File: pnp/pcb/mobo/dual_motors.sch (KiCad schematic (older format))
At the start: 9 parts, among them M5 MOTOR1, M6 MOTOR2

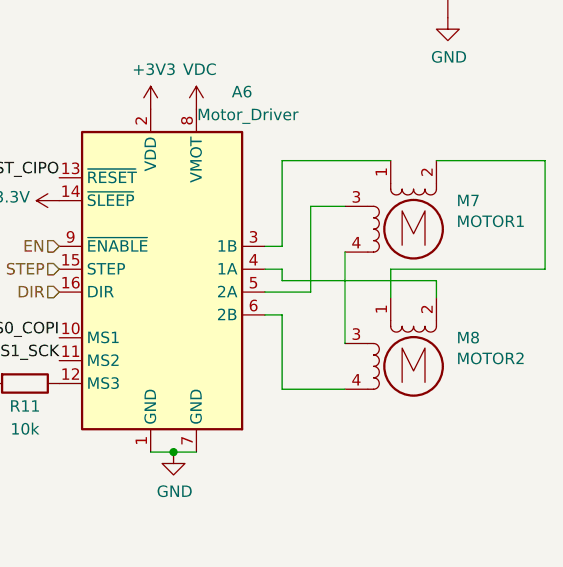
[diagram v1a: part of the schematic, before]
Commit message: Reversed Y and A stepper motor connector
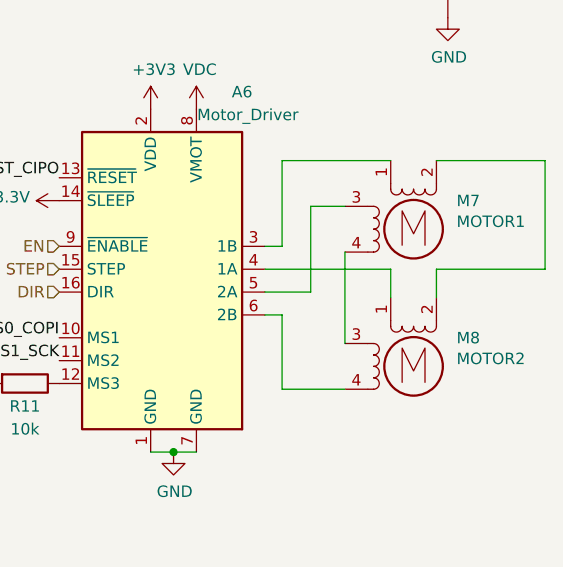
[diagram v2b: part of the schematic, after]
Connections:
- net at M6.1: now also A5.4 (1A); no longer M5.2 (-)
- net at M6.2 (-): now also M5.2 (-); no longer A5.4 (1A)
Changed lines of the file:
@@
 	5725 3250 5925 3250
-Wire Wire Line
-	5800 3150 5725 3150
-Wire Wire Line
-	5800 3200 5800 3150
-Wire Wire Line
-	6475 3200 5800 3200
-Wire Wire Line
-	6475 3275 6475 3200
-Wire Wire Line
-	6275 3150 6275 3275
-Wire Wire Line
-	6950 3150 6275 3150
 Wire Wire Line
 	6950 2675 6950 3150
@@
 	0    1    1    0
 $EndComp
+Wire Wire Line
+	6950 3150 6475 3150
+Wire Wire Line
+	6475 3150 6475 3275
+Wire Wire Line
+	6275 3275 6275 3150
+Wire Wire Line
+	5725 3150 6275 3150
 $EndSCHEMATC

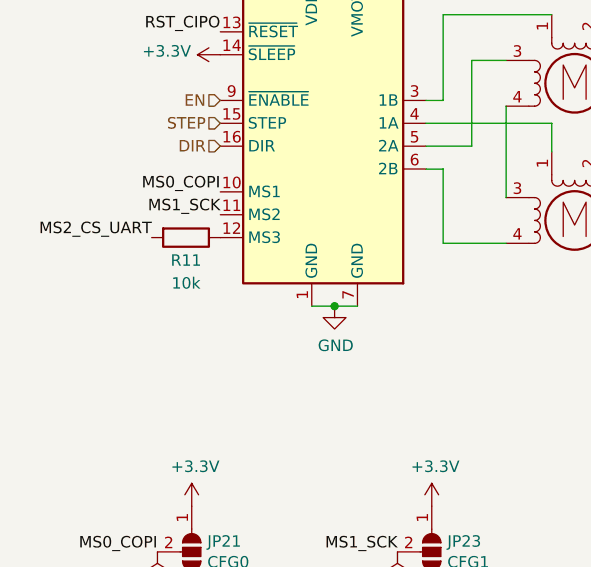
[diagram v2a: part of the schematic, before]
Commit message: Change TMC resistors to 1K
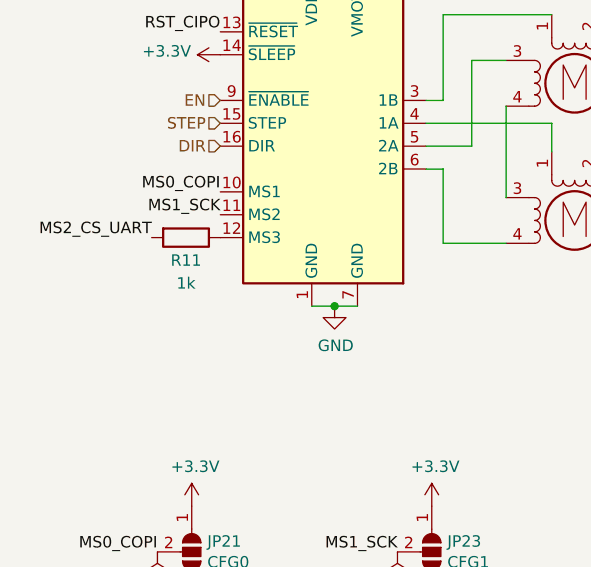
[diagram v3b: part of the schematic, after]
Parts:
- R10: value 10k -> 1k; Digikey RMCF0805FT10K0CT-ND -> (none); JLCPCB C17414 -> C17855; LCSC C115295 -> C322766; Mouser 71-CRCW080510K0FKEAC -> (none)
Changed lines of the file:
@@
 $EndDescr
-$Comp
-L Device:R R?
-U 1 1 6057EB7D
-P 4675 3650
-AR Path="/5EB0C248/6057EB7D" Ref="R?"  Part="1"
-AR Path="/5EB0C248/6057B851/6057EB7D" Ref="R10"  Part="1"
-AR Path="/5EB0C248/60582104/6057EB7D" Ref="R11"  Part="1"
-F 0 "R11" V 4775 3650 50  0000 C CNN
-F 1 "10k" V 4875 3650 50  0000 C CNN
-F 2 "Resistor_SMD:R_0805_2012Metric" V 4605 3650 50  0001 C CNN
-F 3 "" H 4675 3650 50  0001 C CNN
-F 4 "RMCF0805FT10K0CT-ND" H 4675 3650 50  0001 C CNN "Digikey"
-F 5 "C17414" H 4675 3650 50  0001 C CNN "JLCPCB"
-F 6 "C115295" H 4675 3650 50  0001 C CNN "LCSC"
-F 7 "71-CRCW080510K0FKEAC" H 4675 3650 50  0001 C CNN "Mouser"
-	1    4675 3650
-	0    1    1    0
-$EndComp
 $Comp
 L power:+3V3 #PWR?
@@
 Wire Wire Line
 	5725 3150 6275 3150
+$Comp
+L Device:R R?
+U 1 1 61048871
+P 4675 3650
+AR Path="/5EB0C248/61048871" Ref="R?"  Part="1"
+AR Path="/5EB0C248/602A1F7C/61048871" Ref="R?"  Part="1"
+AR Path="/5EB0C248/60347CFB/61048871" Ref="R?"  Part="1"
+AR Path="/5EB0C248/6034863B/61048871" Ref="R?"  Part="1"
+AR Path="/5EB0C248/60348EA3/61048871" Ref="R?"  Part="1"
+AR Path="/5EB0C248/603497CB/61048871" Ref="R?"  Part="1"
+AR Path="/5EB0C248/6035AFD9/61048871" Ref="R?"  Part="1"
+AR Path="/5EB0C248/6036900B/61048871" Ref="R?"  Part="1"
+AR Path="/5EB0C248/6057B851/61048871" Ref="R10"  Part="1"
+AR Path="/5EB0C248/60582104/61048871" Ref="R11"  Part="1"
+F 0 "R11" V 4775 3650 50  0000 C CNN
+F 1 "1k" V 4875 3650 50  0000 C CNN
+F 2 "Resistor_SMD:R_0805_2012Metric" V 4605 3650 50  0001 C CNN
+F 3 "" H 4675 3650 50  0001 C CNN
+F 4 "" H 4675 3650 50  0001 C CNN "Digikey"
+F 5 "C17855" H 4675 3650 50  0001 C CNN "JLCPCB"
+F 6 "C322766" H 4675 3650 50  0001 C CNN "LCSC"
+F 7 "" H 4675 3650 50  0001 C CNN "Mouser"
+	1    4675 3650
+	0    1    1    0
+$EndComp
 $EndSCHEMATC

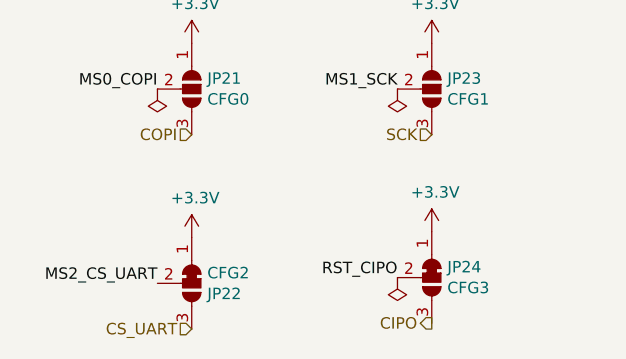
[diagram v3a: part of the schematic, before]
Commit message: Fix default solder jumper configuration
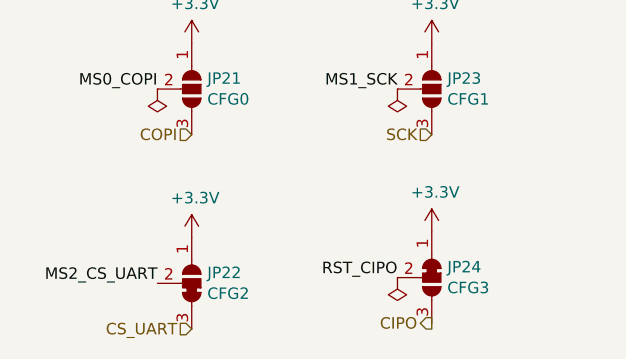
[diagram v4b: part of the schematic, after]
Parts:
- removed JP18: CFG2, Jumper:SolderJumper-3_P1.3mm_Bridged12_RoundedPad1.0x1.5mm, symbol Jumper:SolderJumper_3_Bridged12
- added JP22: CFG2, index:SolderJumper-3_P1.3mm_Bridged23_RoundedPad1.0x1.5mm, symbol index:SolderJumper_3_Bridged23
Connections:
- net +3V3: now also JP22.1 (B)
- net CS_UART: now also JP22.3 (A)
- net MS2_CS_UART: now also JP22.2 (C)
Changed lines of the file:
@@
-$EndComp
-$Comp
-L Jumper:SolderJumper_3_Bridged12 JP?
-U 1 1 6073A4C3
-P 4700 5875
-AR Path="/5EB0C248/602A1F7C/6073A4C3" Ref="JP?"  Part="1"
-AR Path="/5EB0C248/60347CFB/6073A4C3" Ref="JP?"  Part="1"
-AR Path="/5EB0C248/6034863B/6073A4C3" Ref="JP?"  Part="1"
-AR Path="/5EB0C248/60348EA3/6073A4C3" Ref="JP?"  Part="1"
-AR Path="/5EB0C248/6057B851/6073A4C3" Ref="JP18"  Part="1"
-AR Path="/5EB0C248/60582104/6073A4C3" Ref="JP22"  Part="1"
-F 0 "JP22" V 4746 5943 50  0000 L CNN
-F 1 "CFG2" V 4655 5943 50  0000 L CNN
-F 2 "Jumper:SolderJumper-3_P1.3mm_Bridged12_RoundedPad1.0x1.5mm" H 4700 5875 50  0001 C CNN
-F 3 "~" H 4700 5875 50  0001 C CNN
-	1    4700 5875
-	0    1    1    0
 $EndComp
 $Comp
@@
 	0    1    1    0
 $EndComp
+$Comp
+L index:SolderJumper_3_Bridged23 JP22
+U 1 1 6105AE36
+P 4700 5875
+AR Path="/5EB0C248/60582104/6105AE36" Ref="JP22"  Part="1"
+AR Path="/5EB0C248/6057B851/6105AE36" Ref="JP18"  Part="1"
+F 0 "JP22" V 4746 5943 50  0000 L CNN
+F 1 "CFG2" V 4655 5943 50  0000 L CNN
+F 2 "index:SolderJumper-3_P1.3mm_Bridged23_RoundedPad1.0x1.5mm" H 4700 5875 50  0001 C CNN
+F 3 "~" H 4700 5875 50  0001 C CNN
+	1    4700 5875
+	0    1    -1   0
+$EndComp
 $EndSCHEMATC

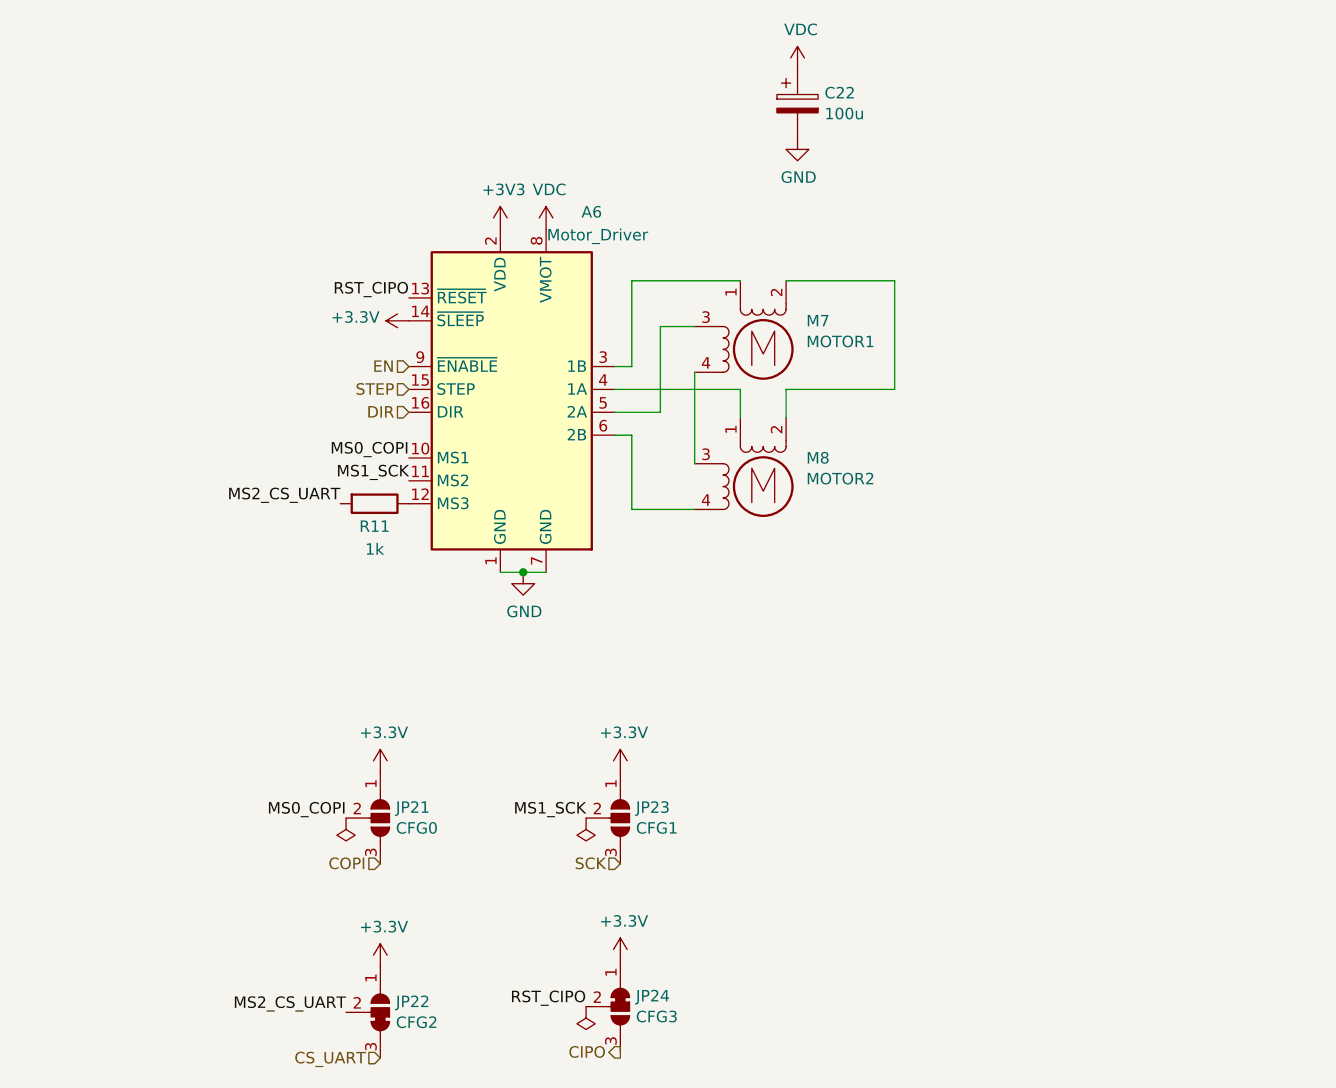
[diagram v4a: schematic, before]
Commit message: changed wiring for stepper drivers that drive two motors from series to parallel. rerouted.
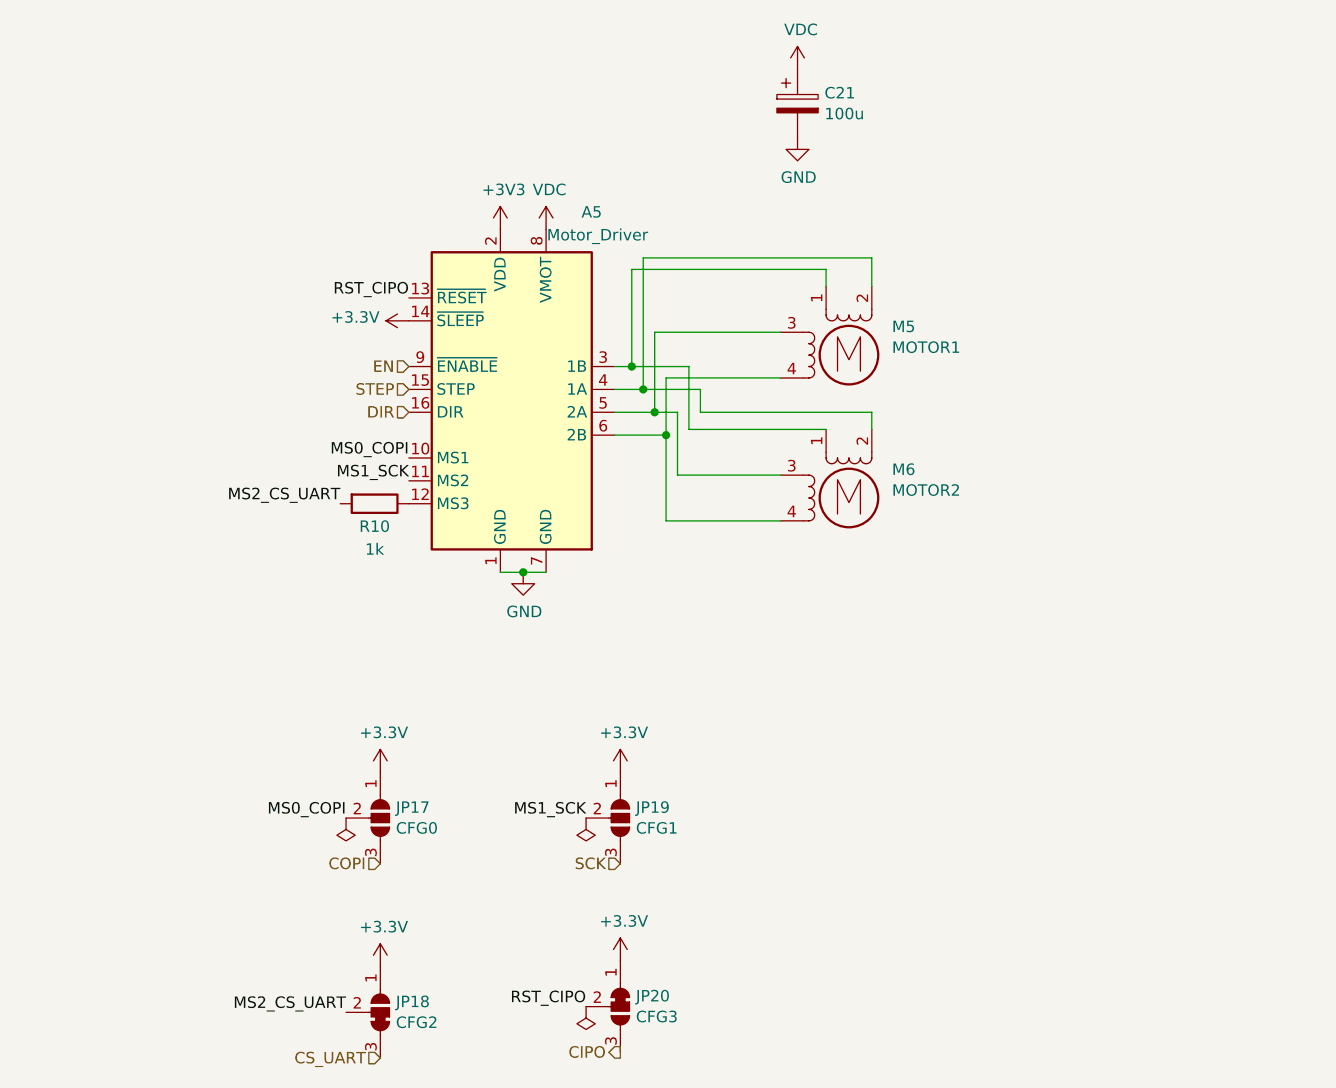
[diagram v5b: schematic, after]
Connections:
- net at M6.1: now also A5.3 (1B), M5.1; no longer A5.4 (1A)
- net at M5.2 (-), M6.2 (-): now also A5.4 (1A)
- net at M6.3: now also A5.5 (2A), M5.3; no longer M5.4
- net at A5.6 (2B), M6.4: now also M5.4
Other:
- moved on the sheet: M5, M6
